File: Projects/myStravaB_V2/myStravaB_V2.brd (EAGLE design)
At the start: 52.3 x 77.5 mm, 103 parts, among them IC1 TPS63051RMWT, Q2 BSS138BKW, T1 BC847, T2 BC847, U1 FXOS8700CQR1, U2 MCP73831, U4 NRF52840, Y2 16MHz, Y3 32.768kHz

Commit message: Final design
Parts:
- added U$8: NET_CONN, NET_CONN:NET_CONN
- moved C34 0.63 mm to (-17.0, 22.6)
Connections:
- new net N$10: C35.2, U$8.2, U4.F23
- net GND: now also U$8.1; no longer C35.2, U4.F23
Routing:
- net N$10: track 0.00 -> 8.52 mm
- net GND: track 82.6 -> 84.0 mm, vias 171 -> 170
- net N$7: track 4.66 -> 3.61 mm

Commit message: Added speaker
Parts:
- added C18: 1uF, rcl:C0603
- added C19: DNP, rcl:C0805
- added R28: 10k, rcl:R0603
- added R29: 330, rcl:R0603
- added T3: BC847, transistor:SOT23
- moved C33 2.40 mm to (10.0, 21.0)
- moved C37 1.02 mm to (-6.22, -25.0)
- moved U$10 0.63 mm to (-14.7, -23.4)
- moved FB1 0.36 mm to (-14.6, 21.1)
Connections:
- removed net XX: U4.G1
- new net N$11: R28.2, T3.1
- new net N$18: C18.2, C19.2
- new net N$6: C18.1, R29.1, T3.3
- new net SPK_IN: R28.1, U4.G1
- net GND: now also C19.1, T3.2
- net VCC: now also R29.2
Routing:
- net SPK_IN: track 0.00 -> 9.99 mm
- net N$6: track 0.00 -> 4.43 mm
- net N$18: track 0.00 -> 2.22 mm
- net N$11: track 0.00 -> 1.63 mm
- net SPI_MI: track 56.5 -> 57.9 mm
- net XL1: track 9.10 -> 10.4 mm
- net GND: track 84.0 -> 84.9 mm, vias 170 -> 174
- net BTND: track 63.4 -> 62.7 mm
- net SPI_SCK: track 67.4 -> 67.9 mm
- net VCC: track 69.7 -> 70.2 mm, vias 42 -> 39

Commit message: Some fuckups corrected
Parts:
- C35: value 820pF -> 0.8pF
- moved C27 5.88 mm to (-7.75, 30.0), turned to 180 degrees
- moved C28 4.58 mm to (-8.00, 22.7), turned to 0 degrees
- moved C33 2.80 mm to (8.26, 23.1)
- moved R28 1.81 mm to (10.5, 17.8)
- moved Y2 1.30 mm to (-7.87, 26.4), turned to 90 degrees
- moved C26 1.14 mm to (-4.19, 26.5)
- moved C32 1.02 mm to (9.91, 19.4)
- moved Y3 1.02 mm to (7.37, 20.7)
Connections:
- removed net YY: U4.J1
- net KILL_NRF: now also U4.A20
- net NEO_PIN: now also U4.J1
- net PPS: no longer U4.L1
- net USB_PRES: now also U4.L1
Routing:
- net NEO_PIN: track 1.75 -> 29.1 mm, vias 0 -> 3
- net PPS: track 23.7 -> 0.00 mm, vias 2 -> 0
- net KILL_NRF: track 1.91 -> 13.4 mm
- net XC2: track 5.99 -> 10.7 mm
- net XC1: track 11.9 -> 8.65 mm
- net SPK_IN: track 9.99 -> 8.12 mm
- net N$11: track 1.63 -> 3.24 mm
- net XL1: track 10.4 -> 8.97 mm
- net SDA: track 83.5 -> 84.1 mm, vias 3 -> 4
- net GND: track 84.9 -> 84.6 mm, vias 174 -> 173

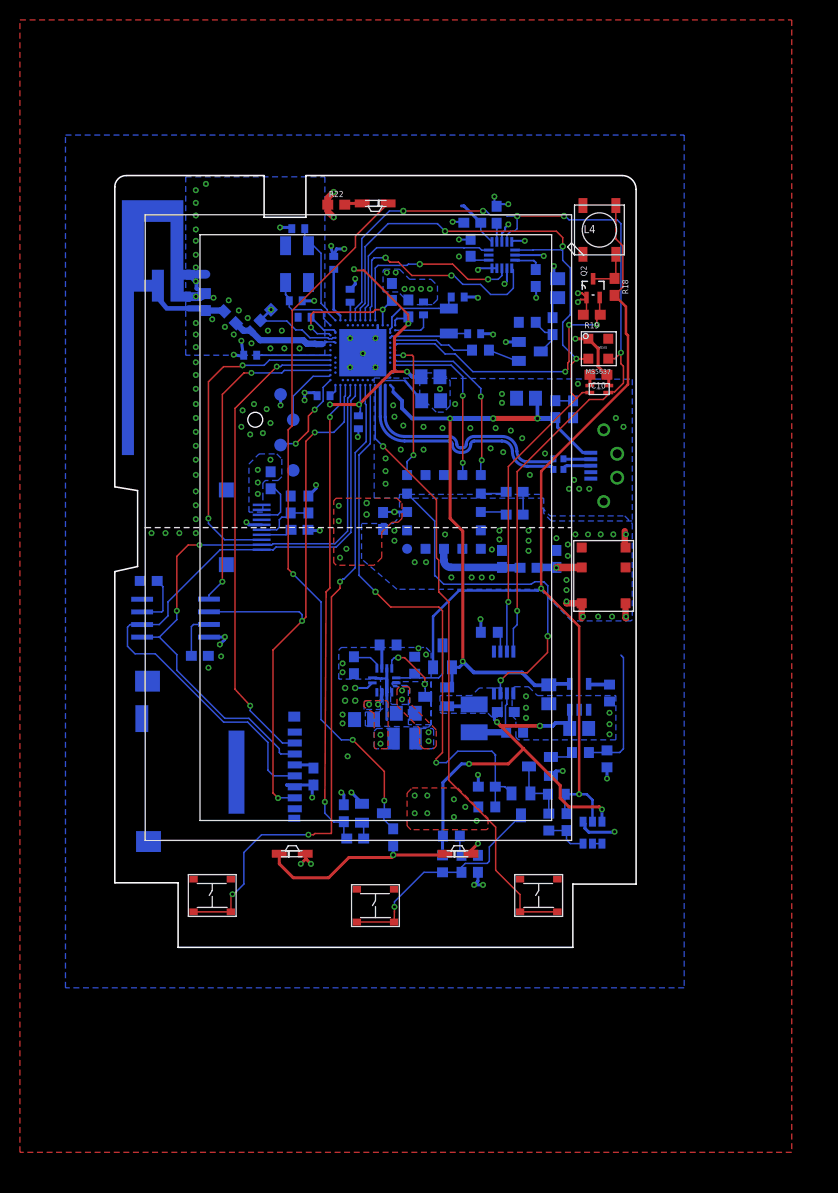
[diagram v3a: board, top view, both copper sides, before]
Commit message: Changed packages Routed USB_PRES
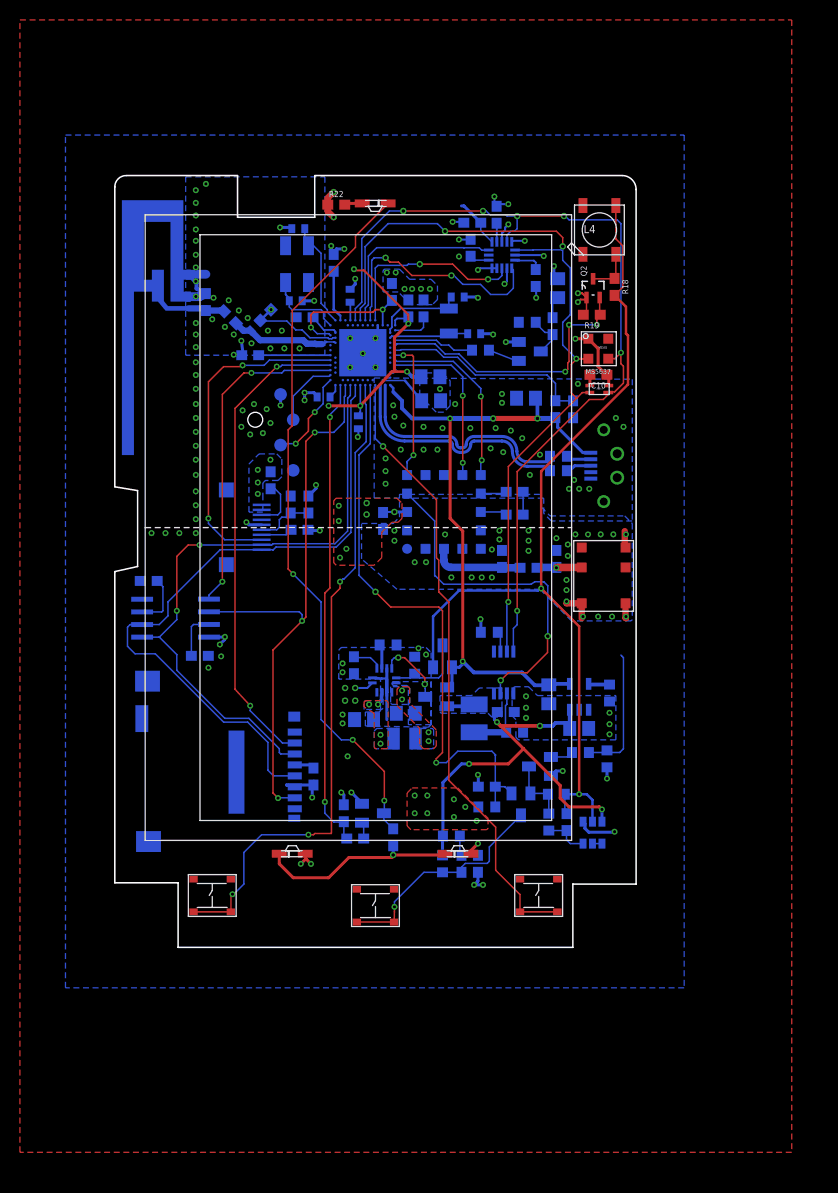
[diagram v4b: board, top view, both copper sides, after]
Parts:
- C2, C24, C26, C29: device rcl:C0402 -> rcl:C0603
- R1, R2: device rcl:R0402 -> rcl:R0603
- moved R2 0.25 mm to (18.4, 7.13)
- moved C30 0.13 mm to (-5.21, 13.1)
- moved R1 0.13 mm to (18.4, 5.68)
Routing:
- net USB_PRES: track 1.79 -> 21.1 mm
- net GND: track 84.6 -> 84.4 mm, vias 173 -> 174
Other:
- outline, holes or cut-outs redrawn

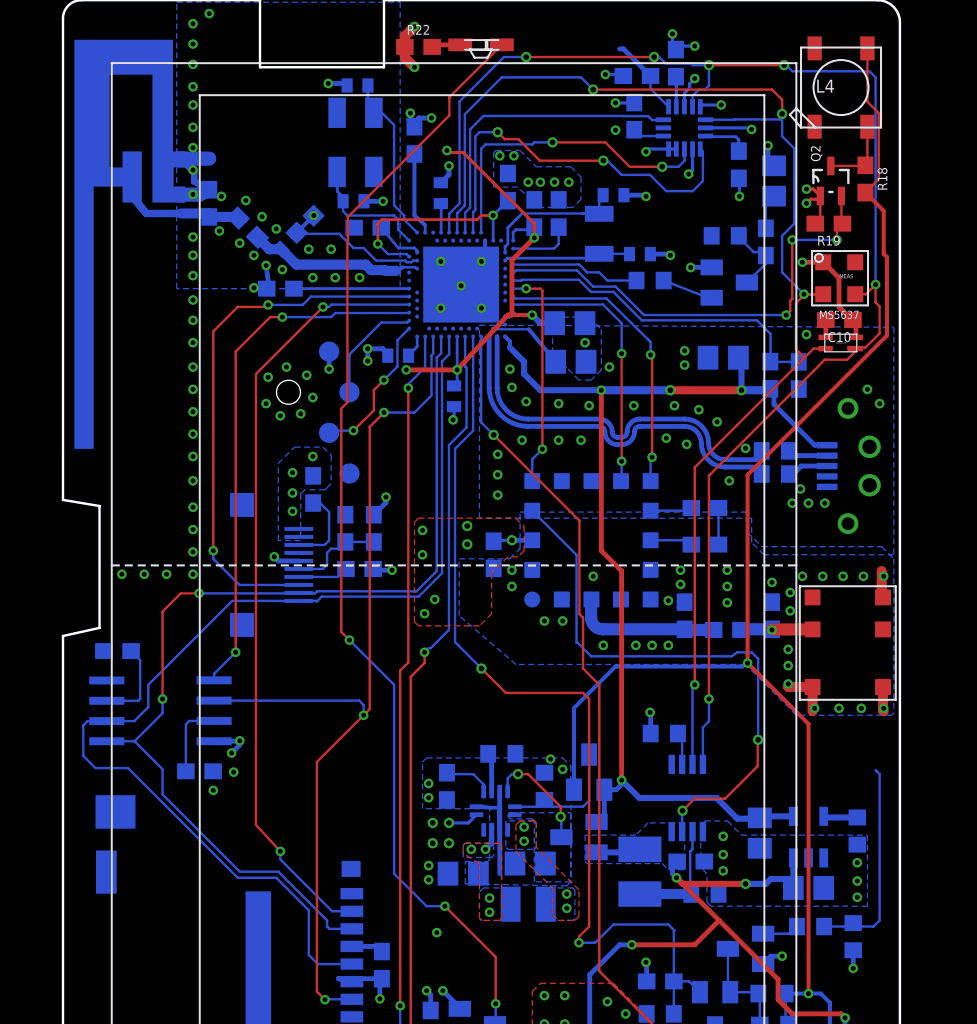
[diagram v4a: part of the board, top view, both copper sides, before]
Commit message: Corrected mistakes on myStravaV10
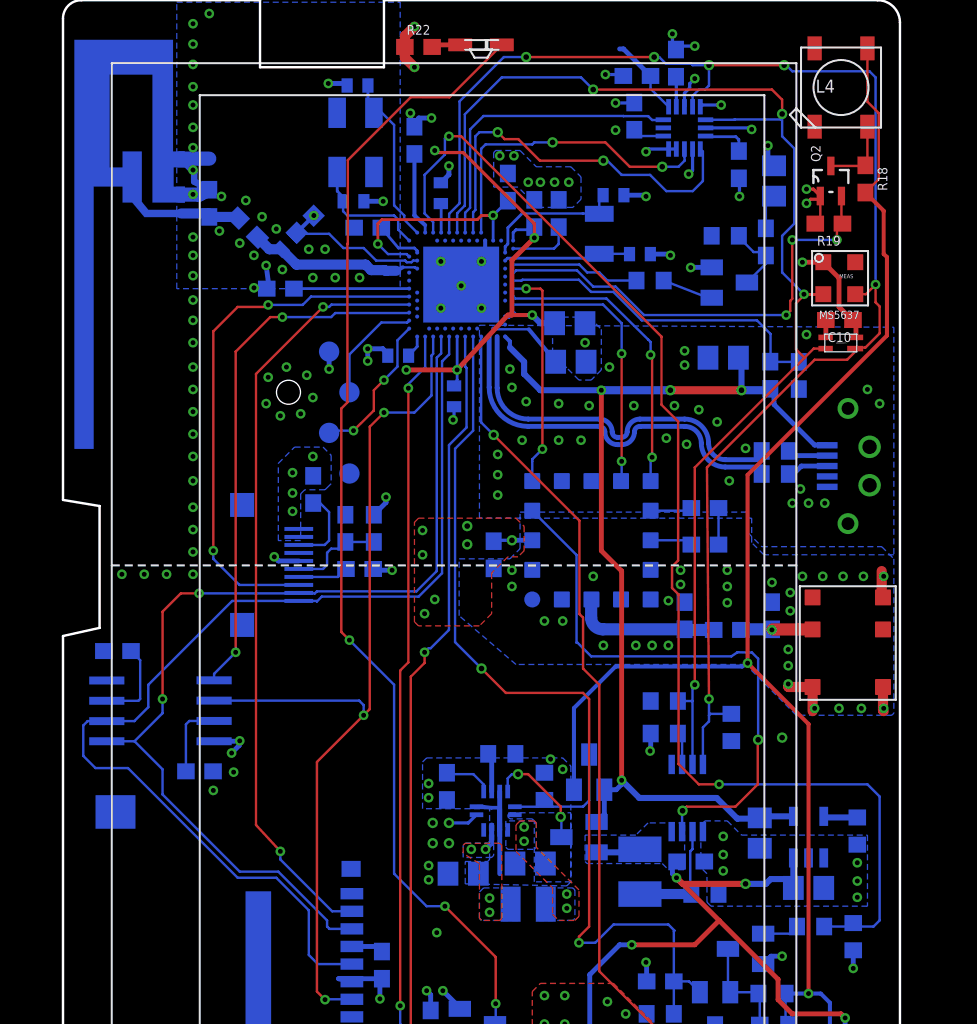
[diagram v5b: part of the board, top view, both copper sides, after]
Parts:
- added R30, R31: 4.7k, rcl:R0603
- Y2: value 16MHz -> 32MHz
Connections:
- net SCL: now also R31.2
- net SDA: now also R30.2
- net VCC: now also R30.1, R31.1
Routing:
- net KILL_NRF: track 13.4 -> 78.0 mm, vias 0 -> 2
- net SCL: track 89.8 -> 91.7 mm
- net BCK_LED_TR: track 72.0 -> 73.4 mm
- net SDA: track 84.1 -> 85.0 mm
- net VCC: track 70.3 -> 71.1 mm, vias 39 -> 40
- net VBAT: track 81.5 -> 82.2 mm

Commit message: Improved version of the bike GPS
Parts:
- removed C18: 1uF, rcl:C0603
- removed C19: DNP, rcl:C0805
- removed D2: BAT54C, diode:SOT23
- removed R28: 10k, rcl:R0603
- removed R29: 330, rcl:R0603
- removed R4: 4.7k, SparkFun-Resistors:0603
- removed R5: 10k, SparkFun-Resistors:0603
- removed T3: BC847, transistor:SOT23
- removed U$10: DM3AT, HIROSE-DM3AT:DM3AT
- moved C29 5.59 mm to (-6.99, 17.3)
- moved R13 2.48 mm to (-8.82, 2.91)
- moved C33 2.32 mm to (9.80, 21.4)
- moved C26 2.15 mm to (-4.60, 24.4)
- moved U$1 1.39 mm to (23.5, -30.6), turned to 270 degrees
- moved R17 1.37 mm to (-7.14, 2.24)
- moved C43 1.17 mm to (-5.56, 2.26)
- moved C32 0.32 mm to (9.80, 19.7)
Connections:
- removed net HW_R: C41.1, U$5.P$7
- removed net HW_S: C40.1, U$5.P$8
- removed net N$11: R28.2, T3.1
- removed net N$18: C18.2, C19.2
- removed net N$6: C18.1, R29.1, T3.3
- removed net N$8: U$1.P$1, U$1.P$2
- removed net SD_CS: U$10.2, U4.U24
- removed net SHARP_CS: U$16.3, U4.R24
- removed net SPK_IN: R28.1, U4.G1
- removed net SW_VBAT: C4.2, D2.2, L4.1-VDD, R10.1, R18.2, U$1.P$5
- removed net USB_PRES: R4.1, R5.2, U4.L1
- new net A2: U4.A8
- new net A3: U4.A10
- new net A99: U4.J24
- new net GPS_RST: C41.1, U$5.P$7, U4.J1
- new net GPS_STDBY: C40.1, U$5.P$8, U4.L1
- new net LS027_CS: U$16.3, U4.AD20
- new net LS027_MO: U$16.2, U4.AD18
- new net LS027_SCK: U$16.1, U4.AD16
- net GND: now also U$1.P$5; no longer C19.1, R5.1, T3.2, U$1.P$4, U$10.6
- net INT1: no longer U4.A8
- net INT2: no longer U4.A10
- net N$15: now also U$1.P$1; no longer U$1.P$3
- net N$9: now also U$1.P$3, U$1.P$6
- net NEO_PIN: now also U4.G1; no longer U4.J1
- net PW_EN: now also C4.2, L4.1-VDD, R10.1, R18.2, U$1.P$4; no longer D2.3
- net SPI_MI: now also U4.R24; no longer U$10.7, U4.AD20
- net SPI_MO: now also U4.L24; no longer U$10.3, U$16.2, U4.AD18
- net SPI_SCK: now also U4.U24; no longer U$10.5, U$16.1, U4.AD16
- net VBAT: now also U$1.P$2; no longer U$1.P$6
- net VCC: no longer R29.2, U$10.4
- net VUSB: no longer D2.1, R4.2
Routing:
- net SW_VBAT: track 89.8 -> 0.00 mm, vias 2 -> 0
- net PW_EN: track 8.03 -> 87.6 mm, vias 0 -> 2
- net SD_CS: track 48.1 -> 0.00 mm, vias 2 -> 0
- net SHARP_CS: track 33.4 -> 0.00 mm, vias 2 -> 0
- net SPI_SCK: track 67.9 -> 40.4 mm, vias 0 -> 2
- net GPS_RST: track 0.00 -> 26.4 mm, vias 0 -> 2
- net LS027_SCK: track 0.00 -> 24.7 mm
- net INT2: track 24.3 -> 0.00 mm, vias 2 -> 0
- net LS027_MO: track 0.00 -> 23.9 mm
- net LS027_CS: track 0.00 -> 23.2 mm
- net GPS_STDBY: track 0.00 -> 23.2 mm, vias 0 -> 2
- net USB_PRES: track 21.1 -> 0.00 mm
- net SPI_MO: track 63.2 -> 43.2 mm
- net INT1: track 19.6 -> 0.00 mm, vias 2 -> 0
- net SPI_MI: track 57.9 -> 39.0 mm, vias 3 -> 2
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
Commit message: Board routed completely:to be checked
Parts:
- removed R6, R7: 4.7k, SparkFun-Resistors:0603
- added C18: 0.1uF, SparkFun-Capacitors:0603
- moved R31 42.9 mm to (-3.07, 28.5), turned to 180 degrees
- moved R30 31.8 mm to (18.1, 22.6), turned to 270 degrees
- moved U$7 29.8 mm to (-23.2, -15.7), turned to 270 degrees
- moved U$2 22.4 mm to (-15.0, 10.8), turned to 180 degrees
- moved C37 2.45 mm to (-4.85, -23.0), turned to 180 degrees
- moved U$1 2.18 mm to (21.7, -31.8), turned to 180 degrees
- moved C43 1.81 mm to (-5.03, 0.53), turned to 90 degrees
- moved R16 1.14 mm to (-7.39, -1.37)
- moved R17 1.01 mm to (-6.50, 1.45)
- moved C29 0.64 mm to (-7.34, 16.7)
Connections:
- removed net A3: U4.A10
- removed net A99: U4.J24
- removed net N$4: R6.2, U$2.WP
- removed net N$5: R7.1, U$2.HOLD
- new net SST_HOLD: U$2.HOLD, U4.AD22
- new net SST_WP: U$2.WP, U4.L24
- net GND: now also C18.2
- net INT1: now also U4.A10
- net PIN_BCK: no longer U4.AD22
- net SPI_MI: now also U4.J24; no longer U4.R24
- net SPI_MO: now also U4.W24; no longer U4.L24
- net SST_CS: now also U4.R24; no longer U4.W24
- net VCC: now also C18.1; no longer R6.1, R7.2
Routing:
- net VCC: track 71.8 -> 162.6 mm, vias 41 -> 40
- net PIN_BCK: track 47.7 -> 1.81 mm, vias 2 -> 0
- net SWDCLK: track 6.98 -> 43.9 mm, vias 0 -> 2
- net SWDIO: track 9.41 -> 42.8 mm
- net SPI_MO: track 43.2 -> 11.3 mm, vias 2 -> 0
- net SPI_SCK: track 40.4 -> 13.2 mm, vias 2 -> 0
- net INT1: track 0.00 -> 21.9 mm
- net SPI_MI: track 39.0 -> 20.2 mm, vias 2 -> 0
- net SST_WP: track 0.00 -> 18.0 mm
- net SST_CS: track 33.6 -> 16.5 mm, vias 2 -> 0
- net N$9: track 3.66 -> 20.6 mm, vias 0 -> 2
- net PW_EN: track 87.6 -> 101.6 mm
- net SST_HOLD: track 0.00 -> 9.90 mm
- net VBAT: track 81.0 -> 72.8 mm
- net GND: track 72.5 -> 65.1 mm, vias 169 -> 196
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- removed copper zone on layer 16, net VCC

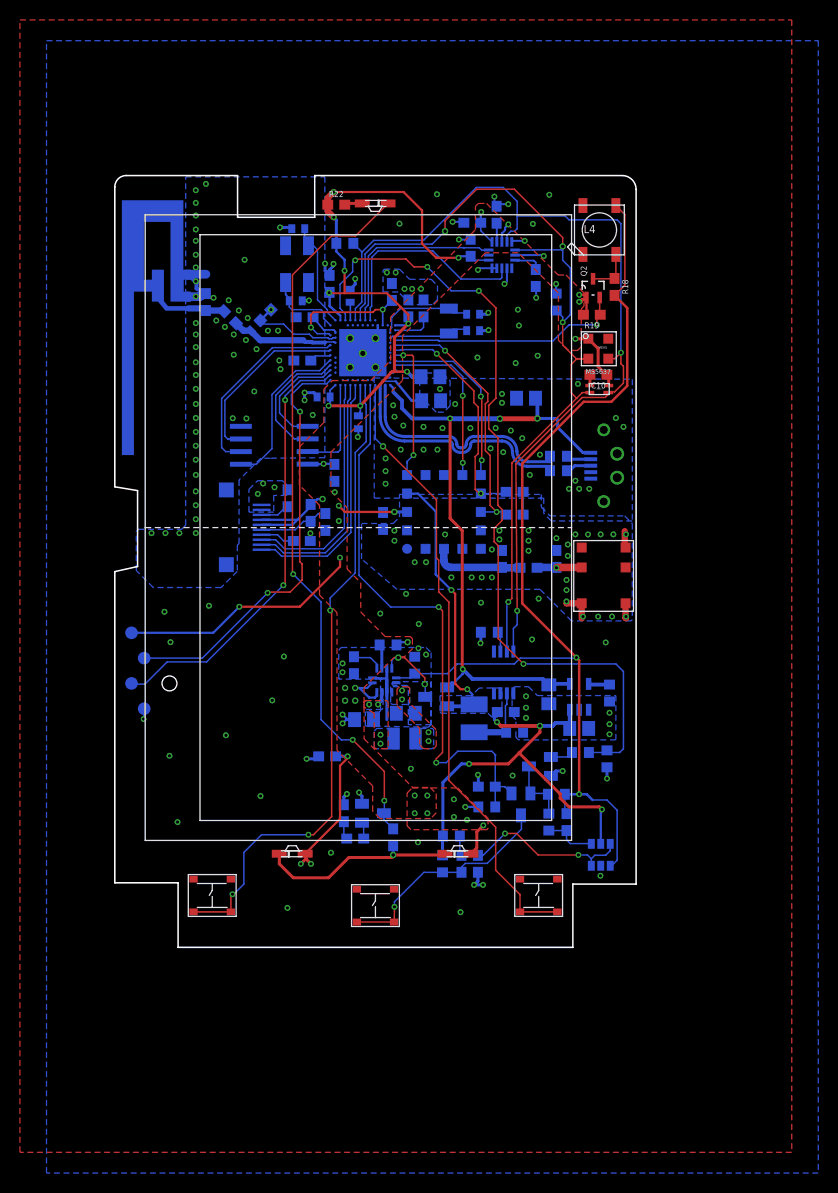
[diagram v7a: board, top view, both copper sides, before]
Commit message: Added small capacitors More vias
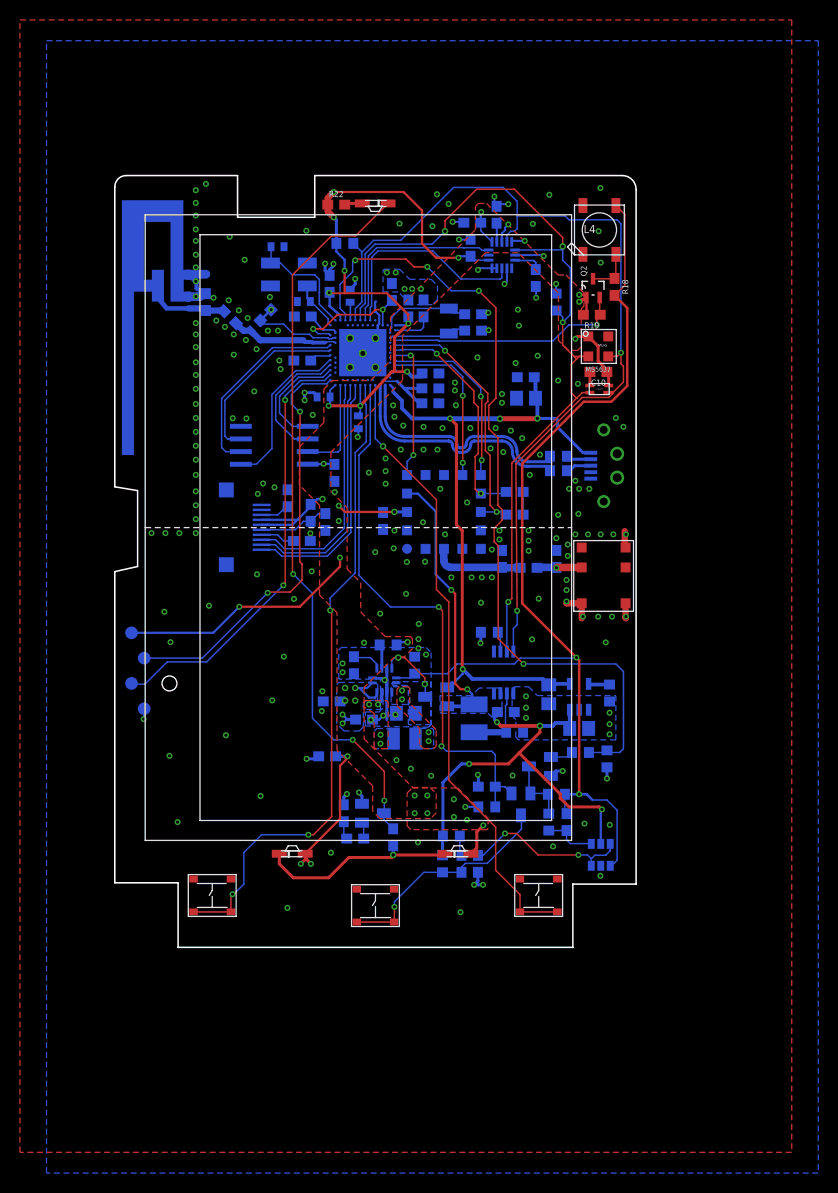
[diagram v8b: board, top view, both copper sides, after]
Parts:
- added C19, C44: 100nF, rcl:C0603
- added C42: 1uF, rcl:C0603
- C12, C17: device rcl:C0805 -> rcl:C0603
- C15, C16: value 12pF -> 4.7uF
- C20: value 4.7uF -> 22uF; device rcl:C0805 -> rcl:C0603
- C32, C33: device rcl:C0402 -> rcl:C0603
- moved C27 2.76 mm to (-9.83, 28.2), turned to 0 degrees
- moved Y2 1.32 mm to (-8.69, 25.4), turned to 0 degrees
- moved C20 1.25 mm to (5.51, 13.9)
- moved C28 0.82 mm to (-7.19, 22.7), turned to 180 degrees
- moved C17 0.33 mm to (5.52, 15.4)
- moved C10 0.28 mm to (22.4, 15.6)
- moved MS1 0.23 mm to (22.4, 18.2)
- moved C24 0.19 mm to (-7.29, 21.2)
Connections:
- net DECUSB: now also C42.1
- net GND: now also C19.2, C42.2, C44.1
- net VCC: now also C44.2
- net VUSB: now also C19.1
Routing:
- net GND: track 65.1 -> 68.9 mm, vias 196 -> 227
- net NRF_BTNC: track 58.7 -> 56.0 mm
- net VUSB: track 66.6 -> 68.8 mm
- net XC1: track 8.65 -> 6.60 mm
- net DECUSB: track 4.88 -> 6.65 mm
- net XC2: track 10.7 -> 12.0 mm
- net DEC4_6: track 14.1 -> 12.9 mm
- net SCL: track 93.6 -> 94.3 mm
- net VCC: track 162.6 -> 163.2 mm
- added copper zone on layer 16, net VCC
